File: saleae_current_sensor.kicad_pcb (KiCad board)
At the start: 2 copper layers, 2 parts, among them U1 AD8541, U2 ACS712xLCTR-05B

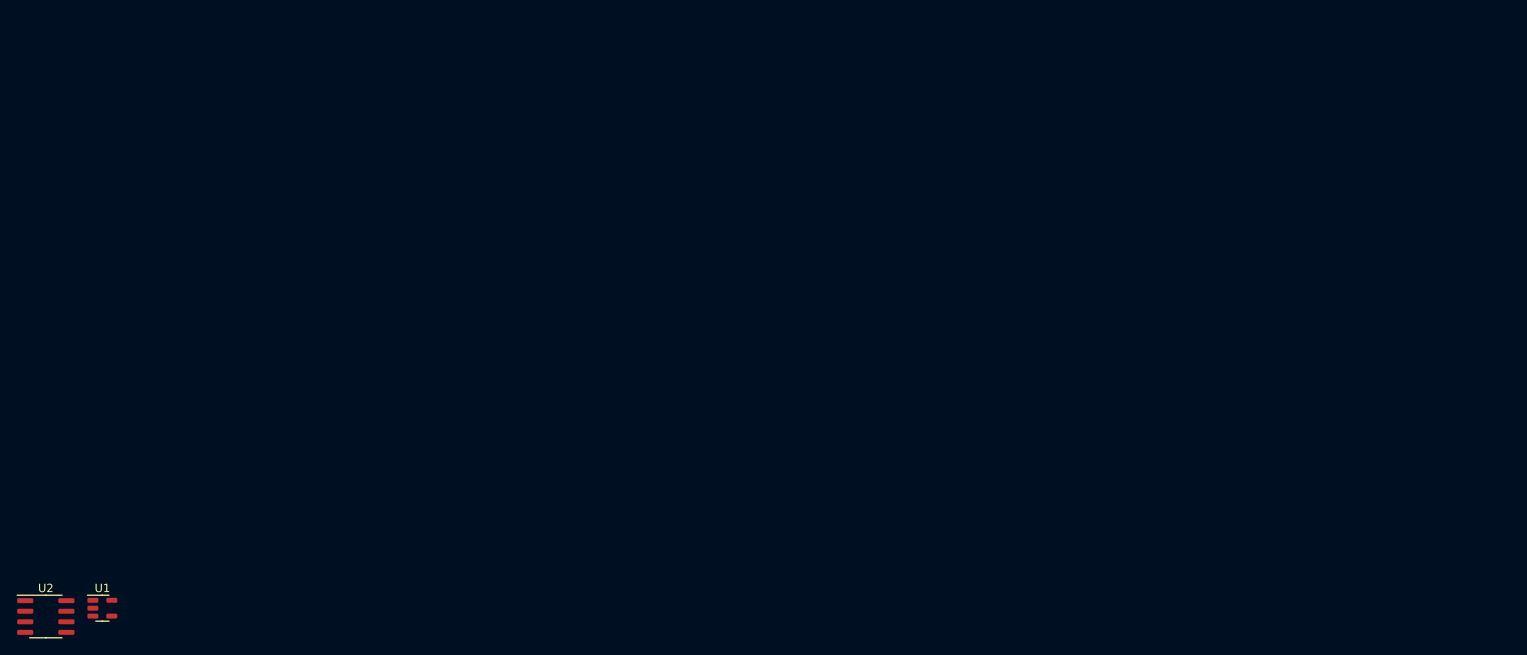
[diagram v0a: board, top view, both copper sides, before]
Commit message: Add buffers to raw signals Add connections for main power lines Annotate all components Assign all footprints
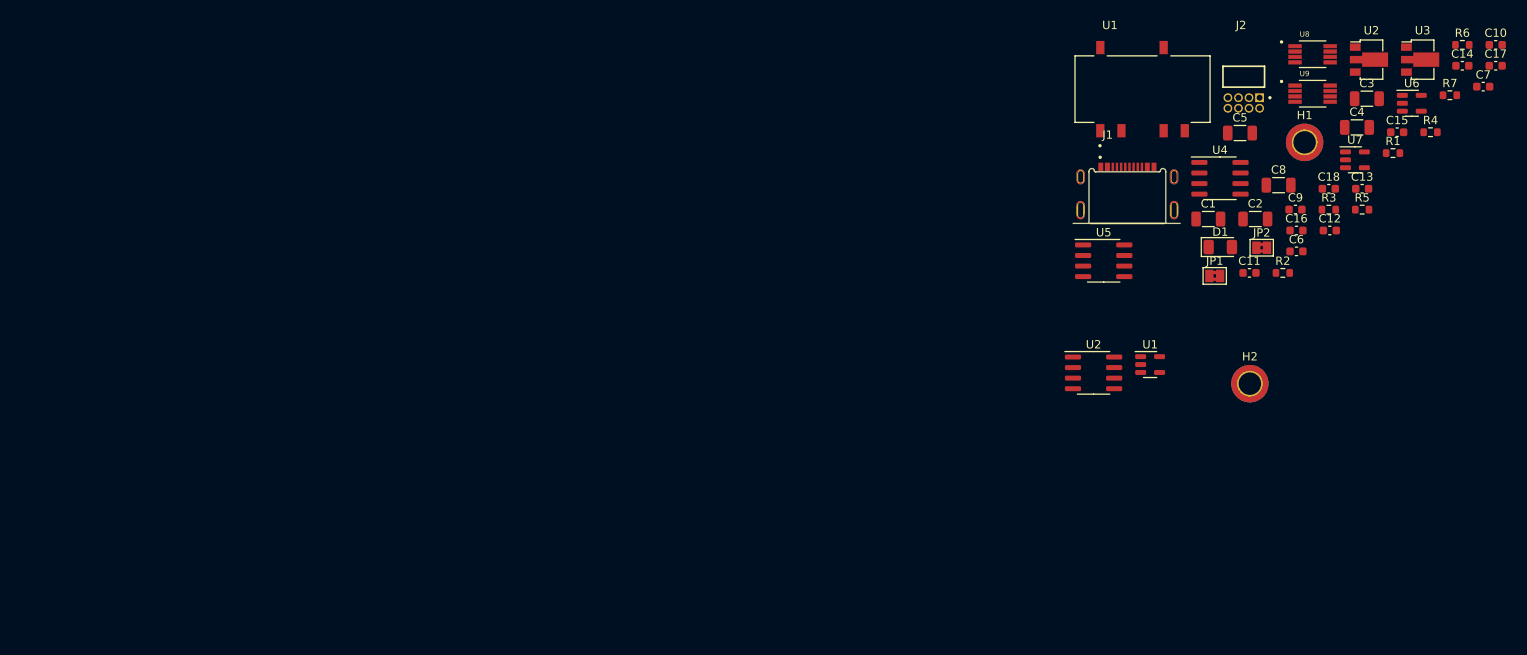
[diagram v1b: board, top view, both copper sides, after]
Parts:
- added C1: 4.7uF, Capacitor_SMD:C_1206_3216Metric, F.Cu at (331.2, 39.0)
- added C10: 100nF, Capacitor_SMD:C_0603_1608Metric, F.Cu at (365.8, 18.1)
- added C11: 100nF, Capacitor_SMD:C_0603_1608Metric, F.Cu at (336.1, 45.5)
- added C12: 100nF, Capacitor_SMD:C_0603_1608Metric, F.Cu at (345.8, 40.4)
- added C13: DNP, Capacitor_SMD:C_0603_1608Metric, F.Cu at (349.7, 35.4)
- added C14: DNP, Capacitor_SMD:C_0603_1608Metric, F.Cu at (361.8, 20.6)
- added C15: 100nF, Capacitor_SMD:C_0603_1608Metric, F.Cu at (353.9, 28.6)
- added C16: 100nF, Capacitor_SMD:C_0603_1608Metric, F.Cu at (341.8, 40.4)
- added C17: 100nF, Capacitor_SMD:C_0603_1608Metric, F.Cu at (365.8, 20.6)
- added C18: 100nF, Capacitor_SMD:C_0603_1608Metric, F.Cu at (345.7, 35.4)
- added C2: 1uF, Capacitor_SMD:C_1206_3216Metric, F.Cu at (336.9, 39.0)
- added C3: 1uF, Capacitor_SMD:C_1206_3216Metric, F.Cu at (350.3, 24.5)
- added C4: 4.7uF, Capacitor_SMD:C_1206_3216Metric, F.Cu at (349.1, 28.0)
- added C5: 4.7uF, Capacitor_SMD:C_1206_3216Metric, F.Cu at (335.0, 28.7)
- added C6: 100nF, Capacitor_SMD:C_0603_1608Metric, F.Cu at (341.8, 42.9)
- added C7: 100nF, Capacitor_SMD:C_0603_1608Metric, F.Cu at (364.3, 23.1)
- added C8: 4.7uF, Capacitor_SMD:C_1206_3216Metric, F.Cu at (339.6, 34.9)
- added C9: 100nF, Capacitor_SMD:C_0603_1608Metric, F.Cu at (341.7, 37.9)
- added D1: LED_Small, LED_SMD:LED_1206_3216Metric, F.Cu at (332.6, 42.4)
- added H1: IP, MountingHole:MountingHole_2.7mm_M2.5_ISO7380_Pad_TopBottom, F.Cu at (342.8, 29.8)
- added H2: IN, MountingHole:MountingHole_2.7mm_M2.5_ISO7380_Pad_TopBottom, F.Cu at (336.2, 58.8)
- added J1: USB4505-03-0-A_REVA, USB4505-03-0-A_REVA:GCT_USB4505-03-0-A_REVA, F.Cu at (321.5, 37.9)
- added J2: FTSH-104-01-SM-D-RA, FTSH-104-01-SM-D-RA:SAMTEC_FTSH-104-01-SM-D-RA, F.Cu at (337.4, 24.4)
- added JP1: SolderJumper_2_Bridged, Jumper:SolderJumper-2_P1.3mm_Bridged2Bar_Pad1.0x1.5mm, F.Cu at (332.0, 45.8)
- added JP2: SolderJumper_2_Bridged, Jumper:SolderJumper-2_P1.3mm_Bridged2Bar_Pad1.0x1.5mm, F.Cu at (337.6, 42.5)
- added R1: 2.5K, Resistor_SMD:R_0603_1608Metric, F.Cu at (353.4, 31.1)
- added R2: 5.1K, Resistor_SMD:R_0603_1608Metric, F.Cu at (340.2, 45.5)
- added R3: 5.1K, Resistor_SMD:R_0603_1608Metric, F.Cu at (345.7, 37.9)
- added R4: 4.7K, Resistor_SMD:R_0603_1608Metric, F.Cu at (357.9, 28.6)
- added R5: 4.7K, Resistor_SMD:R_0603_1608Metric, F.Cu at (349.7, 37.9)
- added R6: 4.95K, Resistor_SMD:R_0603_1608Metric, F.Cu at (361.8, 18.1)
- added R7: 4.95K, Resistor_SMD:R_0603_1608Metric, F.Cu at (360.2, 24.1)
- added U1: TES_1-0523, TES_1-0523:CONV_TES_1-0523, F.Cu at (323.3, 23.4)
- added U2: L78L12, Package_TO_SOT_SMD:SOT-89-3, F.Cu at (350.5, 19.8)
- added U3: L7912, Package_TO_SOT_SMD:SOT-89-3, F.Cu at (356.7, 19.8)
- added U4: ACS723xLCTR-05AB, Package_SO:SOIC-8_3.9x4.9mm_P1.27mm, F.Cu at (332.6, 34.1)
- added U5: ACS723xLCTR-40AB, Package_SO:SOIC-8_3.9x4.9mm_P1.27mm, F.Cu at (318.6, 44.0)
- added U6: LT6015xS5, Package_TO_SOT_SMD:SOT-23-5, F.Cu at (355.7, 25.1)
- added U7: LT6015xS5, Package_TO_SOT_SMD:SOT-23-5, F.Cu at (348.8, 31.9)
- added U8: AD8422, AD8422BRMZ-RL:SOP65P490X110-8N, F.Cu at (343.7, 19.2)
- added U9: AD8422, AD8422BRMZ-RL:SOP65P490X110-8N, F.Cu at (343.7, 23.9)
- moved U1 129.4 mm to (324.2, 56.5)
- moved U2 129.4 mm to (317.4, 57.5)
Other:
- board outline added: 12.9 x 6.6 mm

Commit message: Layout complete
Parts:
- removed the U1 at (324.2, 56.5)
- removed the U2 at (317.4, 57.5)
- added M1: MountingHole_Pad, MountingHole:MountingHole_3.2mm_M3_ISO7380_Pad_TopBottom, F.Cu at (106.7, 74.1)
- added M2: MountingHole_Pad, MountingHole:MountingHole_3.2mm_M3_ISO7380_Pad_TopBottom, F.Cu at (161.7, 74.1)
- added M3: MountingHole_Pad, MountingHole:MountingHole_3.2mm_M3_ISO7380_Pad_TopBottom, F.Cu at (137.8, 106.5)
- J2: value FTSH-104-01-SM-D-RA -> TSM-104-02-T-DH; footprint FTSH-104-01-SM-D-RA:SAMTEC_FTSH-104-01-SM-D-RA -> TSM-104-02-T-DH:SAMTEC_TSM-104-02-T-DH
- moved C10 250.8 mm to (127.7, 97.0), turned to 180 degrees
- moved C14 250.1 mm to (126.8, 106.4), turned to 180 degrees
- moved R7 249.3 mm to (123.7, 102.9), turned to 90 degrees
- moved R6 248.7 mm to (123.0, 87.6), turned to 90 degrees
- moved C17 248.3 mm to (130.9, 101.0), turned to 180 degrees
- moved H1 241.9 mm to (107.4, 85.6)
- moved R4 240.6 mm to (126.0, 92.6)
- moved U6 236.7 mm to (126.6, 84.6)
- moved C7 233.8 mm to (138.4, 83.5), turned to 180 degrees
- moved R5 233.6 mm to (126.8, 108.0)
- moved C12 233.2 mm to (119.8, 97.7), turned to 180 degrees
- moved H2 233.0 mm to (107.4, 102.6)
- moved U7 231.8 mm to (127.1, 99.7)
- moved C15 230.8 mm to (130.3, 85.6), turned to 180 degrees
- moved C13 230.5 mm to (126.1, 91.0), turned to 180 degrees
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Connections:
- J2 pad 01: /VIOUT_5A_SCALED -> GND
- J2 pad 02: GND -> /VIOUT_40A_BUF
- J2 pad 03: /VIOUT_40A_SCALED -> GND
- J2 pad 04: GND -> /VIOUT_5A_BUF
- J2 pad 05: /VIOUT_5A_BUF -> GND
- J2 pad 06: GND -> /VIOUT_40A_SCALED
- J2 pad 07: /VIOUT_40A_BUF -> GND
- J2 pad 08: GND -> /VIOUT_5A_SCALED
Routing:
- net GND: track 0.00 -> 100.8 mm, vias 0 -> 46
- net /VIOUT_5A_BUF: track 0.00 -> 38.8 mm, vias 0 -> 2
- net -12V: track 0.00 -> 34.8 mm, vias 0 -> 3
- net +12V: track 0.00 -> 28.8 mm, vias 0 -> 5
- net +5V: track 0.00 -> 27.0 mm, vias 0 -> 17
- net /VIOUT_40A_BUF: track 0.00 -> 26.9 mm, vias 0 -> 2
- net /VIOUT_40A: track 0.00 -> 23.4 mm
- net /VIOUT_5A: track 0.00 -> 22.7 mm
- net +2V5: track 0.00 -> 18.4 mm, vias 0 -> 2
- net Net-(JP1-Pad1): track 0.00 -> 16.9 mm
- net Net-(JP2-Pad1): track 0.00 -> 12.4 mm
- net -15V: track 0.00 -> 11.5 mm
- net +15V: track 0.00 -> 9.54 mm
- net /VIOUT_5A_SCALED: track 0.00 -> 9.42 mm
- net Net-(J1-PadA5): track 0.00 -> 7.60 mm
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- added copper zone on In2.Cu, net +5V
- added copper zone on In1.Cu, net GND
- added copper zone on B.Cu, net Net-(H1-Pad1)
- added copper zone on F.Cu, net Net-(H1-Pad1)
- added copper zone on In1.Cu, net Net-(H1-Pad1)
- added copper zone on In2.Cu, net Net-(H1-Pad1)
- added copper zone on B.Cu, net Net-(H2-Pad1)
- added copper zone on F.Cu, net Net-(H2-Pad1)
- added copper zone on In1.Cu, net Net-(H2-Pad1)
- added copper zone on In2.Cu, net Net-(H2-Pad1)
- added copper zone on B.Cu, net Net-(U4-Pad3)
- added copper zone on F.Cu, net Net-(U4-Pad3)
- added copper zone on In1.Cu, net Net-(U4-Pad3)
- added copper zone on In2.Cu, net Net-(U4-Pad3)
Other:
- board size 12.9 x 6.6 mm -> 64 x 40.4 mm
- copper layers 2 -> 4
- board text added: "+-05A: -10 to +10V, 2V/A +-40A: -10 to +10V, 250mV/A"
- board text added: "05A RAW"
- board text added: "05A SCALED"
- board text added: "40A RAW"
- board text added: "40A SCALED"
- board text added: "GND"
- board text added: "HIGH VOLTAGE"
- board text added: "POS CURRENT +-40A MAX"
- board text added: "REV: ${REVISION}"
